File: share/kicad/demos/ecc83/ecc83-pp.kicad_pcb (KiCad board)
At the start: 2 copper layers, 44.5 x 41.9 mm, 15 parts, among them P1 IN, P2 OUT, P3 POWER, P4 CONN_2, P5 CONN_1, P6 CONN_1, P7 CONN_1, P8 CONN_1, U1 ECC83

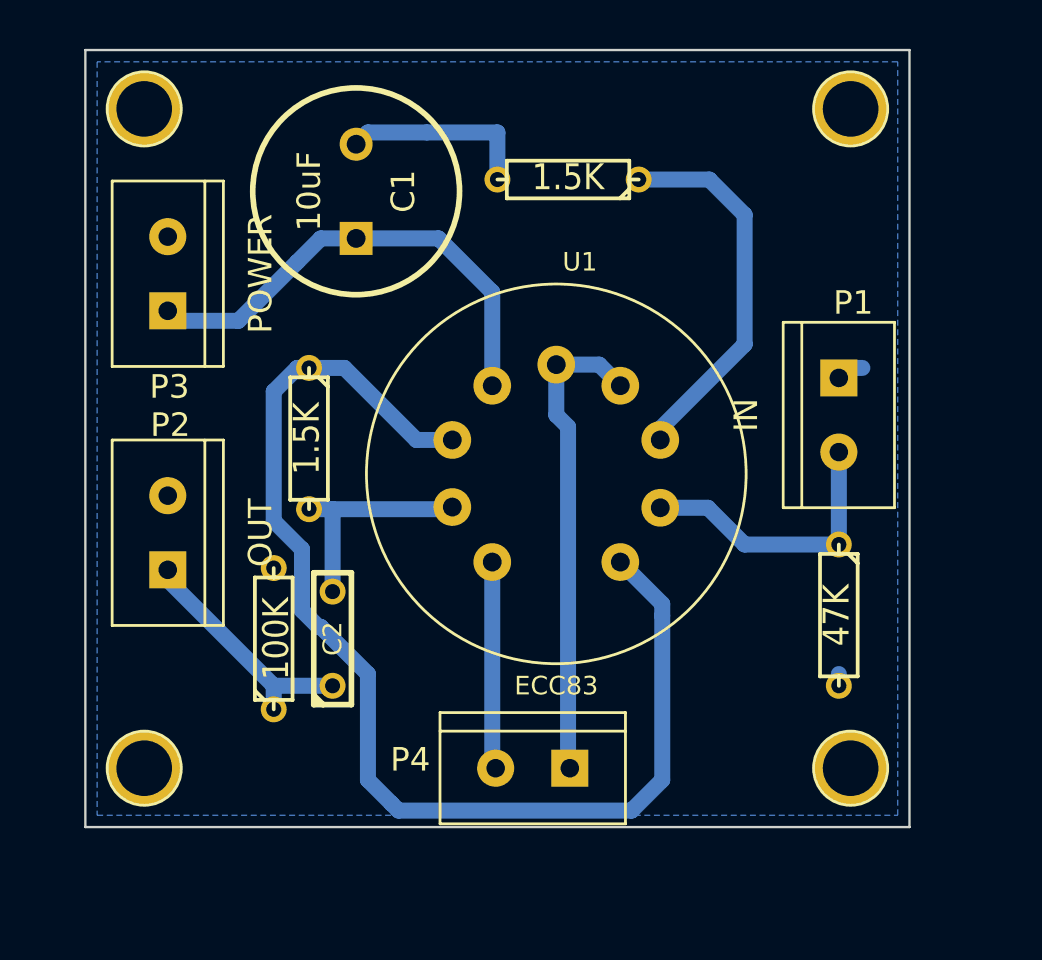
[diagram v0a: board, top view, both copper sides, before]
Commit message: Remove KiCad V4.0.7
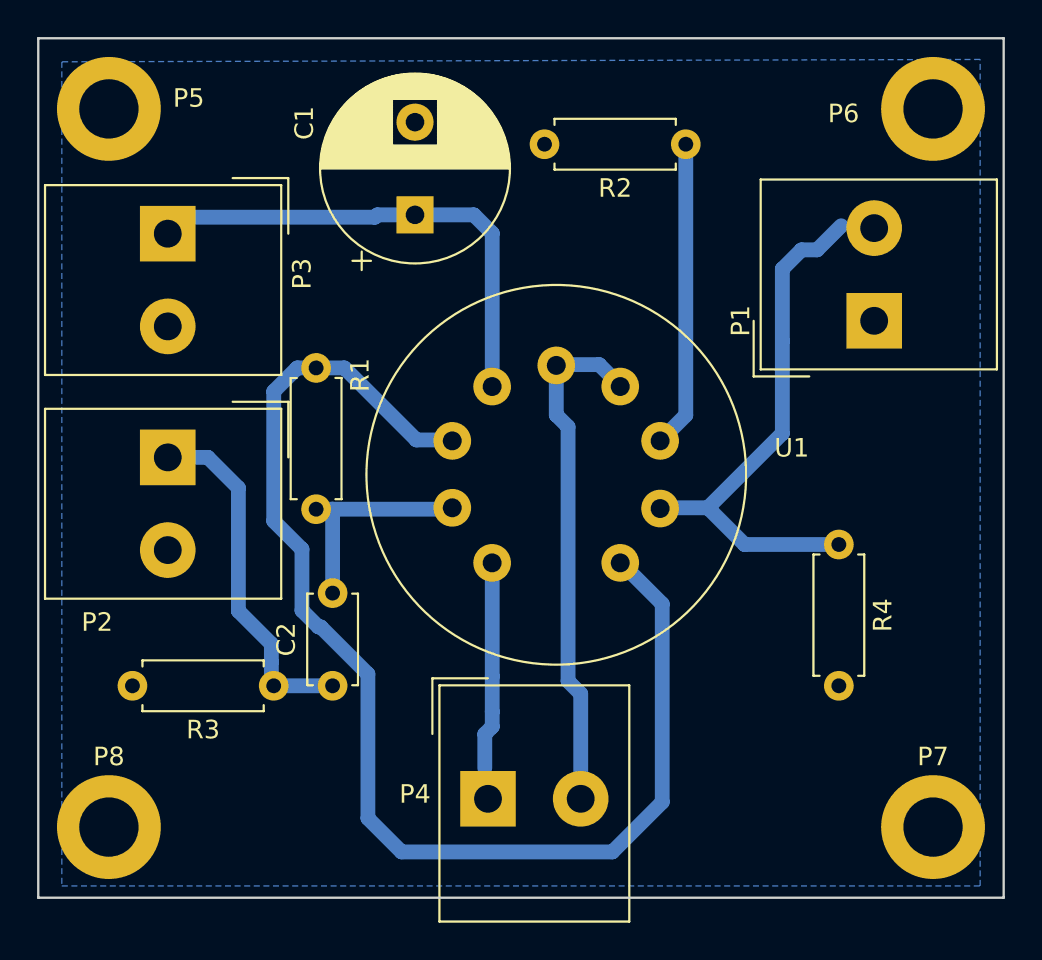
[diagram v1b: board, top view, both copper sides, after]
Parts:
- C1: footprint discret:C2V10 -> Capacitor_THT:CP_Radial_D10.0mm_P5.00mm
- C2: footprint discret:C2 -> Capacitor_THT:C_Disc_D4.7mm_W2.5mm_P5.00mm
- P1, P2, P3, P4: footprint connect:bornier2 -> TerminalBlock_Altech:Altech_AK300_1x02_P5.00mm_45-Degree
- P5, P6, P7, P8: value CONN_1 -> MOUNTING_HOLE; footprint connect:1pin -> MountingHole:MountingHole_3.2mm_M3_DIN965_Pad
- R1, R2, R3, R4: footprint discret:R3 -> Resistor_THT:R_Axial_DIN0207_L6.3mm_D2.5mm_P7.62mm_Horizontal
- U1: footprint Valves:VALVE-ECC-83-1 -> Valve:Valve_ECC-83-1
- moved R2 6.63 mm to (156.2, 95.9)
- moved P7 5.46 mm to (169.5, 132.7)
- moved P1 5.43 mm to (166.4, 105.4), turned to 90 degrees
- moved P6 4.44 mm to (169.5, 94.0)
- moved P2 4.06 mm to (128.3, 112.8), turned to -90 degrees
- moved R1 3.83 mm to (136.3, 108.0)
- moved R4 3.81 mm to (164.5, 117.5)
- moved P8 3.70 mm to (125.1, 132.7)
- moved C1 3.42 mm to (141.6, 99.7)
- moved P4 2.92 mm to (145.5, 131.2), turned to 0 degrees
- moved C2 2.54 mm to (137.2, 125.1)
- moved R3 2.54 mm to (134.0, 125.1), turned to 180 degrees
- moved P3 2.16 mm to (128.3, 100.7), turned to -90 degrees
- moved P5 1.91 mm to (125.1, 94.0)
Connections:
- P5 pad 1: Net-(P5-Pad1) -> (no net)
- P6 pad 1: Net-(P6-Pad1) -> (no net)
- P7 pad 1: Net-(P7-Pad1) -> (no net)
- P8 pad 1: Net-(P8-Pad1) -> (no net)
- U1 pad 4: Net-(P4-Pad1) -> Net-(P4-Pad2)
- U1 pad 5: Net-(P4-Pad1) -> Net-(P4-Pad2)
- U1 pad 9: Net-(P4-Pad2) -> Net-(P4-Pad1)
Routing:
- net Net-(P4-Pad2): track 11.3 -> 27.9 mm
- net Net-(P4-Pad1): track 26.2 -> 11.3 mm
- net Net-(P1-Pad2): track 14.9 -> 29.1 mm
- net GND: track 12.3 -> 0.00 mm
- net Net-(C2-Pad1): track 12.5 -> 19.1 mm
- net Net-(R2-Pad1): track 20.5 -> 16.6 mm
- net Net-(R1-Pad1): track 64.8 -> 68.6 mm
- net Net-(C1-Pad1): track 25.6 -> 26.6 mm
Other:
- board size 44.5 x 41.9 mm -> 52.1 x 46.4 mm
- net class Default removed
- rule pad_to_mask_clearance: 0.1 -> 0
